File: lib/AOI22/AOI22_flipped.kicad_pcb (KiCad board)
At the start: 2 copper layers, 8 parts, among them P1 Q_PJFET_GSD, P2 Q_PJFET_GSD, P3 Q_PJFET_GSD, P4 Q_PJFET_GSD

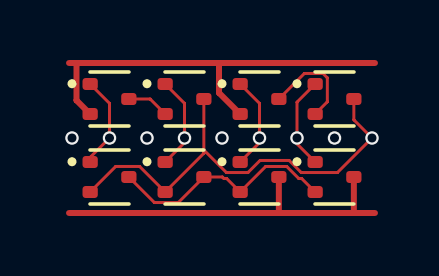
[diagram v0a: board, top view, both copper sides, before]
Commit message: Move pin definition to gate's physical .v
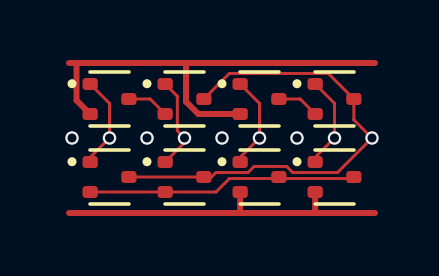
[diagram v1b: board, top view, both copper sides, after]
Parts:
- N1, N2, N3, N4: value Q_NJFET_GSD -> (none)
- P1, P2, P3, P4: value Q_PJFET_GSD -> (none)
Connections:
- net A renamed A1
- net B renamed A2
- net C renamed B1
- net D renamed B2
- net Net-(N1-D) renamed intA
- net Net-(N3-D) renamed intB
- P1 pad 2: Y -> intP
- P1 pad 3: Net-(P1-D) -> Y
- P2 pad 2: Y -> intP
- P2 pad 3: Net-(P1-D) -> Y
- P3 pad 2: Net-(P1-D) -> VDD
- P3 pad 3: VDD -> intP
- P4 pad 2: Net-(P1-D) -> VDD
- P4 pad 3: VDD -> intP
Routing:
- net intP: track 0.00 -> 9.04 mm
- net Net-(P1-D): track 7.83 -> 0.00 mm
- net intB: track 3.40 -> 1.42 mm
- net GND: track 14.1 -> 15.4 mm
- net VDD: track 12.6 -> 11.7 mm
- net Y: track 15.1 -> 16.1 mm

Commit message: High-density layout with pitch of 1.1mm, which gains 23% !!
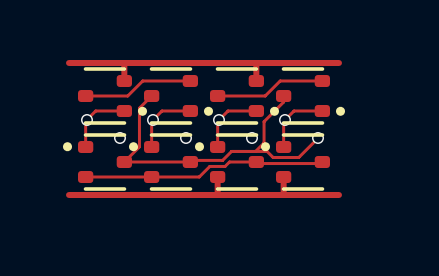
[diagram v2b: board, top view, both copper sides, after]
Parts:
- moved P4 1.16 mm to (7.70, 3.30)
- moved N4 1.05 mm to (7.70, 1.10), turned to 180 degrees
- moved P3 0.90 mm to (5.50, 3.30)
- moved N3 0.76 mm to (5.50, 1.10), turned to 180 degrees
- moved P2 0.67 mm to (3.30, 3.30)
- moved P1 0.52 mm to (1.10, 3.30)
- moved N2 0.46 mm to (3.30, 1.10), turned to 180 degrees
- moved N1 0.18 mm to (1.10, 1.10), turned to 180 degrees
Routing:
- net GND: track 15.4 -> 10.2 mm
- net Y: track 16.1 -> 12.6 mm
- net intA: track 1.42 -> 3.70 mm
- net intB: track 1.42 -> 3.70 mm
- net VDD: track 11.7 -> 10.2 mm
- net intP: track 9.04 -> 8.14 mm
- net B1: track 3.13 -> 2.29 mm
- net A2: track 3.13 -> 2.29 mm
- net B2: track 3.13 -> 2.29 mm
- net A1: track 3.13 -> 2.29 mm
- net (no net): vias 4 -> 3

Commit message: All cells now use 1mm*4mm grid rather than 1.1mm*4.4mm
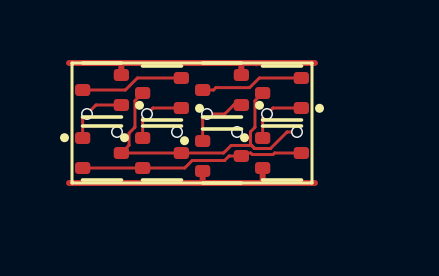
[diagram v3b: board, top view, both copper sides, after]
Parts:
- moved P4 0.76 mm to (7.00, 3.00)
- moved N4 0.71 mm to (7.00, 1.00)
- moved N3 0.54 mm to (5.00, 0.90)
- moved P3 0.54 mm to (5.00, 3.10)
- moved P2 0.42 mm to (3.00, 3.00)
- moved N2 0.32 mm to (3.00, 1.00)
- moved P1 0.32 mm to (1.00, 3.00)
- moved N1 0.22 mm to (1.00, 0.90)
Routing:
- net Y: track 12.6 -> 10.9 mm
- net VDD: track 10.2 -> 9.11 mm
- net GND: track 10.2 -> 9.13 mm
- net intP: track 8.14 -> 7.50 mm

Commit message: Make the pads of my SOT523 footprint very slightly smaller, which is enough to route all the cells and leave the mosfets exactly on the grid
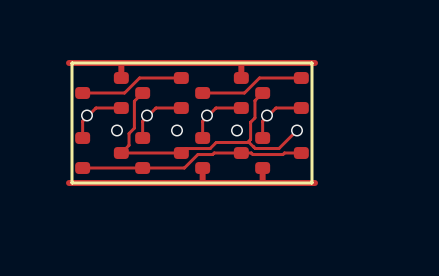
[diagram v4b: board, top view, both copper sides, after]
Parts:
- N1, N2, N3, N4, P1, P2, P3, P4: footprint Package_TO_SOT_SMD:SOT-523 -> RV523:SOT523
- moved P3 0.10 mm to (5.00, 3.00)
- moved N1 0.10 mm to (1.00, 1.00)
- moved N3 0.10 mm to (5.00, 1.00)

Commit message: Propagate MOSFET values to the cells' PCBs
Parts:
- N1, N2, N3, N4: value (none) -> NMOS
- P1, P2, P3, P4: value (none) -> PMOS
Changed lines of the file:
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@@
 			)
 		)
-		(property "Value" ""
+		(property "Value" "PMOS"
 			(at 0 0 0)
 			(layer "F.Fab")
@@
 			)
 		)
-		(property "Value" ""
+		(property "Value" "PMOS"
 			(at 0 0 0)
 			(layer "F.Fab")
@@
 			)
 		)
-		(property "Value" ""
+		(property "Value" "PMOS"
 			(at 0 0 0)
 			(layer "F.Fab")
@@
 			)
 		)
-		(property "Value" ""
+		(property "Value" "NMOS"
 			(at 0 0 180)
 			(layer "F.Fab")
@@
 			)
 		)
-		(property "Value" ""
+		(property "Value" "NMOS"
 			(at 0 0 180)
 			(layer "F.Fab")
@@
 			)
 		)
-		(property "Value" ""
+		(property "Value" "NMOS"
 			(at 0 0 180)
 			(layer "F.Fab")
@@
 			)
 		)
-		(property "Value" ""
+		(property "Value" "NMOS"
 			(at 0 0 180)
 			(layer "F.Fab")
@@
 			)
 		)
-		(property "Value" ""
+		(property "Value" "PMOS"
 			(at 0 0 0)
 			(layer "F.Fab")
